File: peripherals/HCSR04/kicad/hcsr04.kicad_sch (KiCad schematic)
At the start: 12 parts

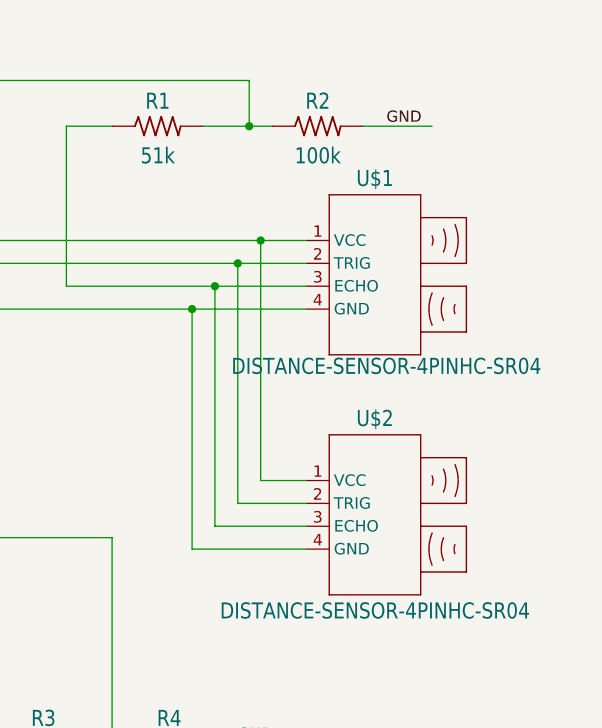
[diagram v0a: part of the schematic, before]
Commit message: Adding README for HC-SR04
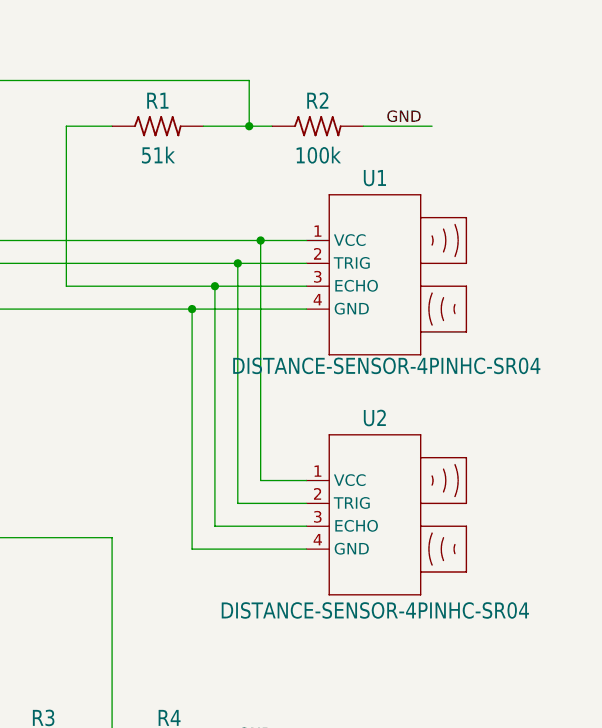
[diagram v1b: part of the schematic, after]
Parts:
- renumbered U$1 to U1, U$2 to U2
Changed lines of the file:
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@@
 (kicad_sch
-	(version 20231120)
+	(version 20250114)
 	(generator "eeschema")
-	(generator_version "8.0")
+	(generator_version "9.0")
 	(paper "A4")
 	(junction
@@
 	(label "GND"
 		(at 182.88 152.4 0)
-		(fields_autoplaced yes)
 		(effects
 			(font
@@
 	(label "GND"
 		(at 139.7 76.2 90)
-		(fields_autoplaced yes)
 		(effects
 			(font
@@
 	(label "PIO2"
 		(at 149.86 78.74 90)
-		(fields_autoplaced yes)
 		(effects
 			(font
@@
 	(label "PIO1"
 		(at 152.4 78.74 90)
-		(fields_autoplaced yes)
 		(effects
 			(font
@@
 	(label "VIN"
 		(at 142.24 76.2 90)
-		(fields_autoplaced yes)
 		(effects
 			(font
@@
 	(label "GND"
 		(at 199.39 83.82 0)
-		(fields_autoplaced yes)
 		(effects
 			(font
@@
 	(label "PIO3"
 		(at 147.32 78.74 90)
-		(fields_autoplaced yes)
 		(effects
 			(font
@@
 	(label "PIO4"
 		(at 144.78 78.74 90)
-		(fields_autoplaced yes)
 		(effects
 			(font
@@
 		(on_board yes)
 		(dnp no)
-		(property "Reference" "U$2"
+		(property "Reference" "U2"
 			(at 198.12 117.348 0)
 			(effects
@@
 			(project ""
 				(path "/e914310d-c3d7-4877-a217-210efc1ca858"
-					(reference "U$2")
+					(reference "U2")
 					(unit 1)
 				)
@@
 		(on_board yes)
 		(dnp no)
-		(property "Reference" "U$1"
+		(property "Reference" "U1"
 			(at 198.12 90.678 0)
 			(effects
@@
 			(project ""
 				(path "/e914310d-c3d7-4877-a217-210efc1ca858"
-					(reference "U$1")
+					(reference "U1")
 					(unit 1)
 				)
@@
 		)
 	)
+	(embedded_fonts no)
 )

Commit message: Completing HC-SR04 peripheral, and other minor changes.
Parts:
- JP1, JP2: Placement (none) -> short/straight post is soldered to board; Type (none) -> through hole
- JP3, JP4, JP5, JP6: Type (none) -> through hole
- R1, R2, R3, R4: Package (none) -> radial; Type (none) -> through hole
- U1, U2: Manufacturer (none) -> Olimex LTD; Mfg Part # (none) -> SNS-HCSR04; Type (none) -> through hole
